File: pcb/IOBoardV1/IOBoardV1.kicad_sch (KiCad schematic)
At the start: 13 parts, among them J1 XT60PW-M, J2 TYPE-C-31-M-12, J3 L8AL-1X1T-32A, J4 L8AL-1X1T-32A, J5 Conn_01x04_Pin

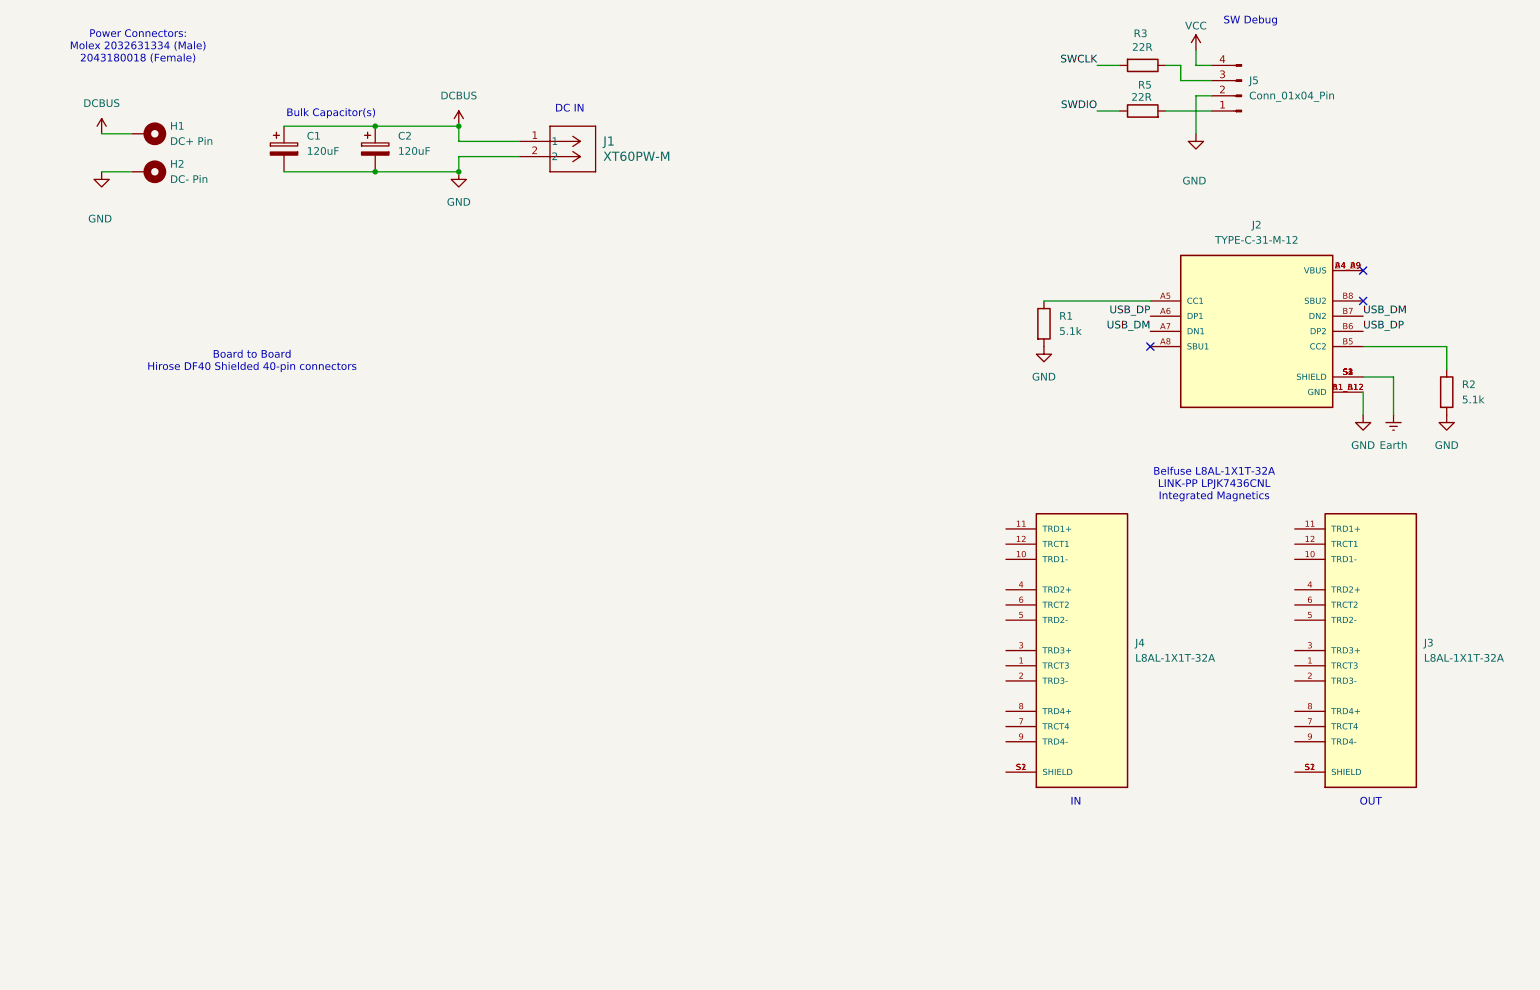
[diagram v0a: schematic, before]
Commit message: schematic finished, need to set proper ERCs
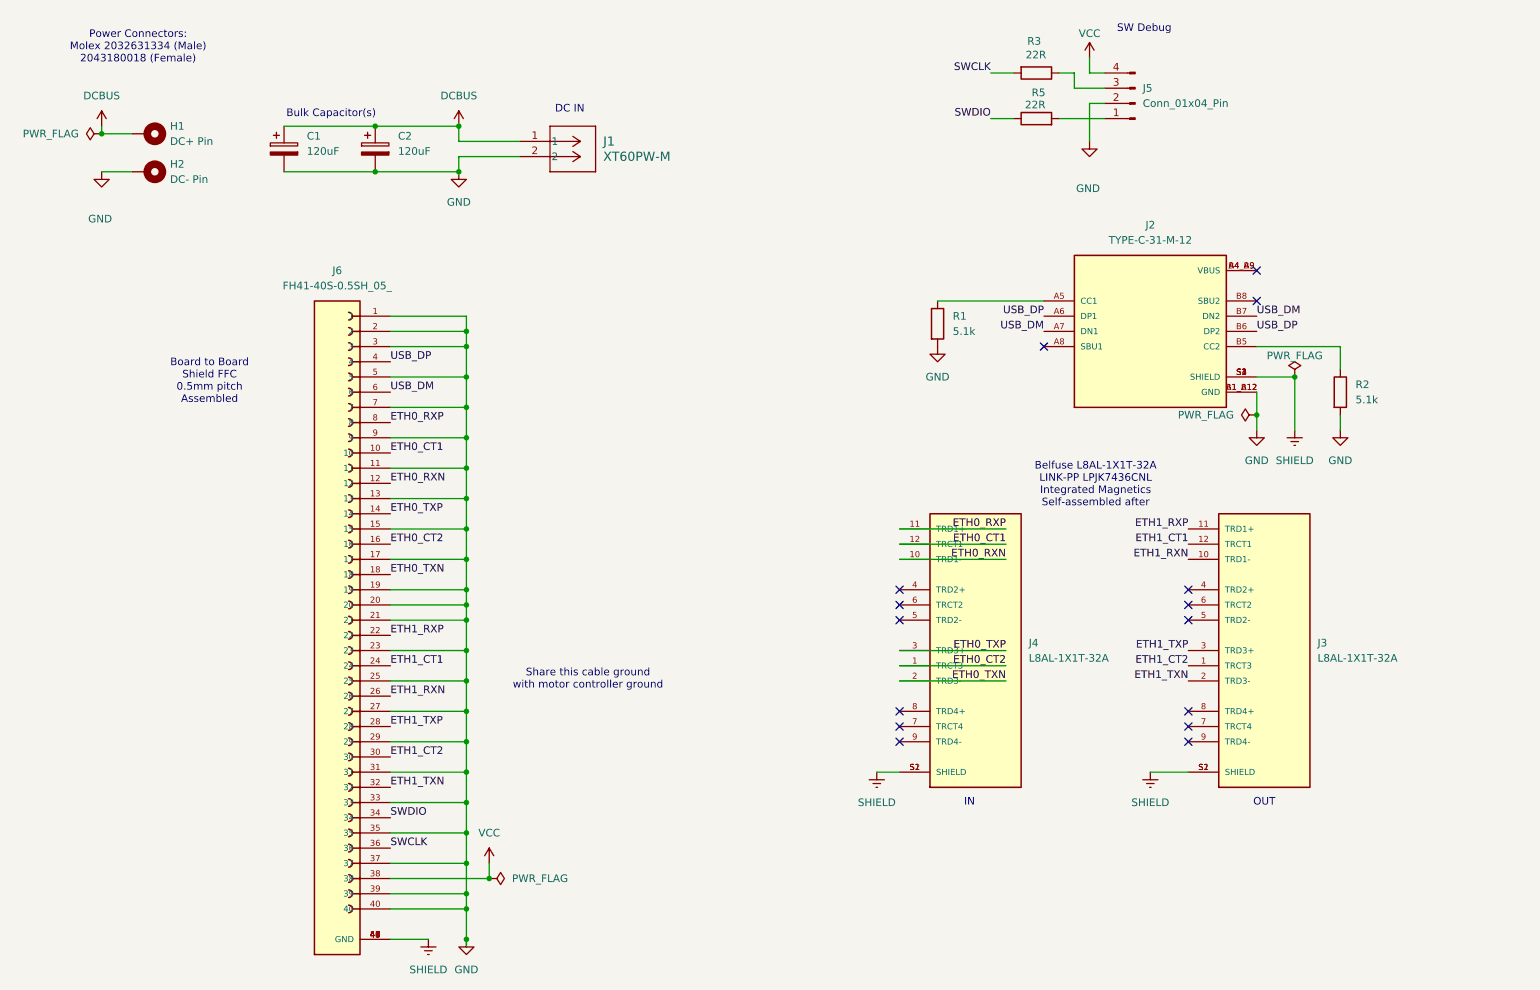
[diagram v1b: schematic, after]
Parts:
- added J6: FH41-40S-0.5SH_05_, FH41-40S-0.5SH_05_:HRS_FH41-40S-0.5SH_05_, symbol FH41-40S-0.5SH_05_:FH41-40S-0.5SH_05_
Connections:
- net Earth is gone; now on net SHIELD: J2.S1 (SHIELD), J2.S2 (SHIELD), J2.S3 (SHIELD), J2.S4 (SHIELD)
- net GND: now also J6.1, J6.11, J6.13, J6.15, J6.17, J6.19, J6.2, J6.20, J6.21, J6.23, J6.25, J6.27, J6.29, J6.3, J6.31, J6.33, J6.35, J6.37, J6.39, J6.40, J6.5, J6.7, J6.9
- net SWCLK: now also J6.36
- net SWDIO: now also J6.34
- net USB_DM: now also J6.6
- net USB_DP: now also J6.4
- net VCC: now also J6.38
- net ETH1_CT2: now reaches J3.1 (TRCT3)
- net ETH1_CT2: now also J6.30
- net ETH1_RXN: now reaches J3.10 (TRD1-)
- net ETH1_RXN: now also J6.26
- net ETH1_RXP: now reaches J3.11 (TRD1+)
- net ETH1_RXP: now also J6.22
- net ETH1_CT1: now reaches J3.12 (TRCT1)
- net ETH1_CT1: now also J6.24
- net ETH1_TXN: now reaches J3.2 (TRD3-)
- net ETH1_TXN: now also J6.32
- net ETH1_TXP: now reaches J3.3 (TRD3+)
- net ETH1_TXP: now also J6.28
- net SHIELD: now reaches J3.S1 (SHIELD), J3.S2 (SHIELD)
- net SHIELD: now also J4.S1 (SHIELD), J4.S2 (SHIELD), J6.41 (GND), J6.42 (GND), J6.43 (GND), J6.44 (GND), J6.45 (GND), J6.46 (GND), J6.47 (GND), J6.48 (GND), J6.49 (GND), J6.50 (GND)
- net ETH0_CT2: now reaches J4.1 (TRCT3)
- net ETH0_CT2: now also J6.16
- net ETH0_RXN: now reaches J4.10 (TRD1-)
- net ETH0_RXN: now also J6.12
- net ETH0_RXP: now reaches J4.11 (TRD1+)
- net ETH0_RXP: now also J6.8
- net ETH0_CT1: now reaches J4.12 (TRCT1)
- net ETH0_CT1: now also J6.10
- net ETH0_TXN: now reaches J4.2 (TRD3-)
- net ETH0_TXN: now also J6.18
- net ETH0_TXP: now reaches J4.3 (TRD3+)
- net ETH0_TXP: now also J6.14
- no-connect marks 3 -> 15
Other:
- note added: "Belfuse L8AL-1X1T-32A LINK-PP LPJK7436CNL Integrated Magnetics Self-assembled after"
- note added: "Board to Board Shield FFC 0.5mm pitch Assembled"
- note added: "Share this cable ground with motor controller ground"
- note removed: "Belfuse L8AL-1X1T-32A LINK-PP LPJK7436CNL Integrated Magnetics"
- note removed: "Board to Board Hirose DF40 Shielded 40-pin connectors"
- moved on the sheet: J2, J3, J4, J5, R1, R2, R3, R5

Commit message: Added more BOM items
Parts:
- removed J3: L8AL-1X1T-32A, L8AL-1X1T-32A:BEL_L8AL-1X1T-32A, symbol L8AL-1X1T-32A:L8AL-1X1T-32A
- C1, C2: value 120uF -> 100V 330uF; LCSC Part Number (none) -> C783453
- J4: value L8AL-1X1T-32A -> DNP; LCSC Part Number (none) -> LINK-PP LPJK7436CNL
- J5: value Conn_01x04_Pin -> Right Angle 1x4; LCSC Part Number (none) -> C91552
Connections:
- net ETH0_CT2: now also J4.6 (TRCT2); no longer J4.1 (TRCT3)
- net ETH0_TXN: now also J4.5 (TRD2-); no longer J4.2 (TRD3-)
- net ETH0_TXP: now also J4.4 (TRD2+); no longer J4.3 (TRD3+)
- net ETH1_CT1: now also J4.1 (TRCT3)
- net ETH1_CT2: now also J4.7 (TRCT4)
- net ETH1_RXN: now also J4.2 (TRD3-)
- net ETH1_RXP: now also J4.3 (TRD3+)
- net ETH1_TXN: now also J4.9 (TRD4-)
- net ETH1_TXP: now also J4.8 (TRD4+)
- no-connect marks 15 -> 3
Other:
- note added: "Belfuse L8AL-1X1T-32A LINK-PP LPJK7436CNL Integrated Magnetics Purchased Separately"
- note removed: "Belfuse L8AL-1X1T-32A LINK-PP LPJK7436CNL Integrated Magnetics Self-assembled after"
- note removed: "IN"
- note removed: "OUT"
- moved on the sheet: J4
